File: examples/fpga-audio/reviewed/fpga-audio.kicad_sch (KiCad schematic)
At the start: 29 parts, among them J1 3V3 IN, J2 AUDIO OUT, J3 SPI PROG, U1 iCE40UP5K, U2 PCM5102A, U3 AP2112K-1.2, U4 W25Q32JV, X1 12MHz

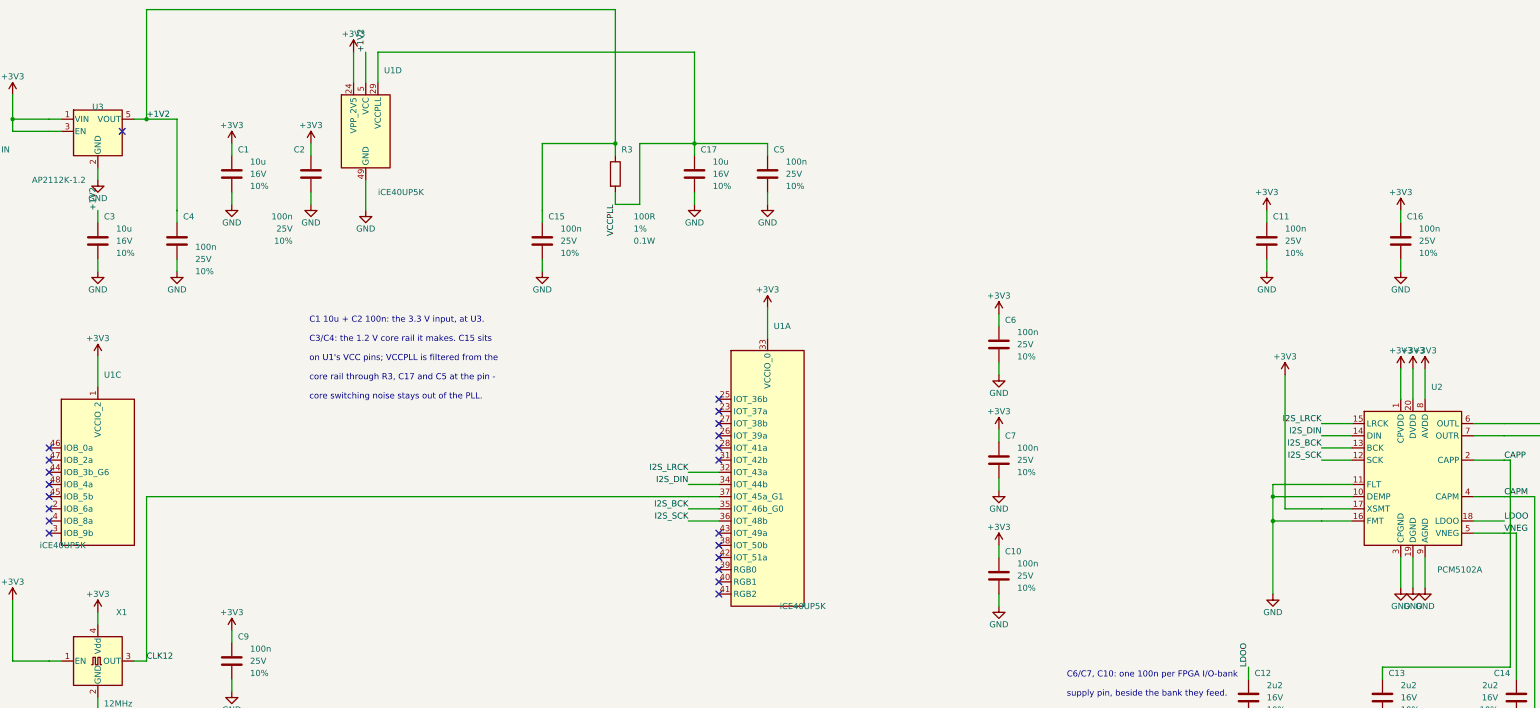
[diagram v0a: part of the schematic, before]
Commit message: Measure the copper that goes out and comes back, and the text drawn on text
The reviewer sent screenshots with circles on them. Two kinds: strings
printed through each other on the schematics, and copper that leaves a
pad, travels three sides of a rectangle and arrives four millimetres
away. Neither had a rule that could see it - `text_over_wire` measured
text against nets and nothing measured text against text, and
`route.detour` weighs a whole net, which averages one bad connection
away under any ratio worth setting.

New rule `route.wander`: one continuous run of copper - pad or junction
at each end - against the shortest way between those two ends that
clears the packages in between. The baseline walks the perimeter of
whatever the straight line crosses, so an opamp's feedback wrap is
measured against going round the package rather than through it. On
KiCad's 18 demo boards it fires once at the shipped 2.0x.

`readability.text_over_text` and `_over_wire` are regraded info: they
fire on 14 and 10 of those 18 human sheets. That is the estimate
talking, not the drawing. `ai-generated` still promotes both to errors,
so every generated design has to have none - and the five examples do.

What the two rules then made us fix:

* a net label's anchor cannot move, but its reading direction can. Each
  name is now offered the four quarters of its anchor and takes the
  first that prints over nothing. Power symbol names and PWR_FLAG names
  get the same treatment - four grounds on one row printed GNGNGNGND.
  Schematic text overlaps: buck 1, motor 2, carrier 1, fpga 7, all to 0.
* a plane crossing was priced at forty times front copper per
  millimetre, which is a prohibition, not a price: one millimetre of
  crossing bought a forty millimetre tour and the boards had grown
  them. Thirty is where neither `route.wander` nor `route.return_path`
  fires. Buck, motor and carrier now have no wander findings.
* `write_variant` resolves the routes a second time, so the
  straight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
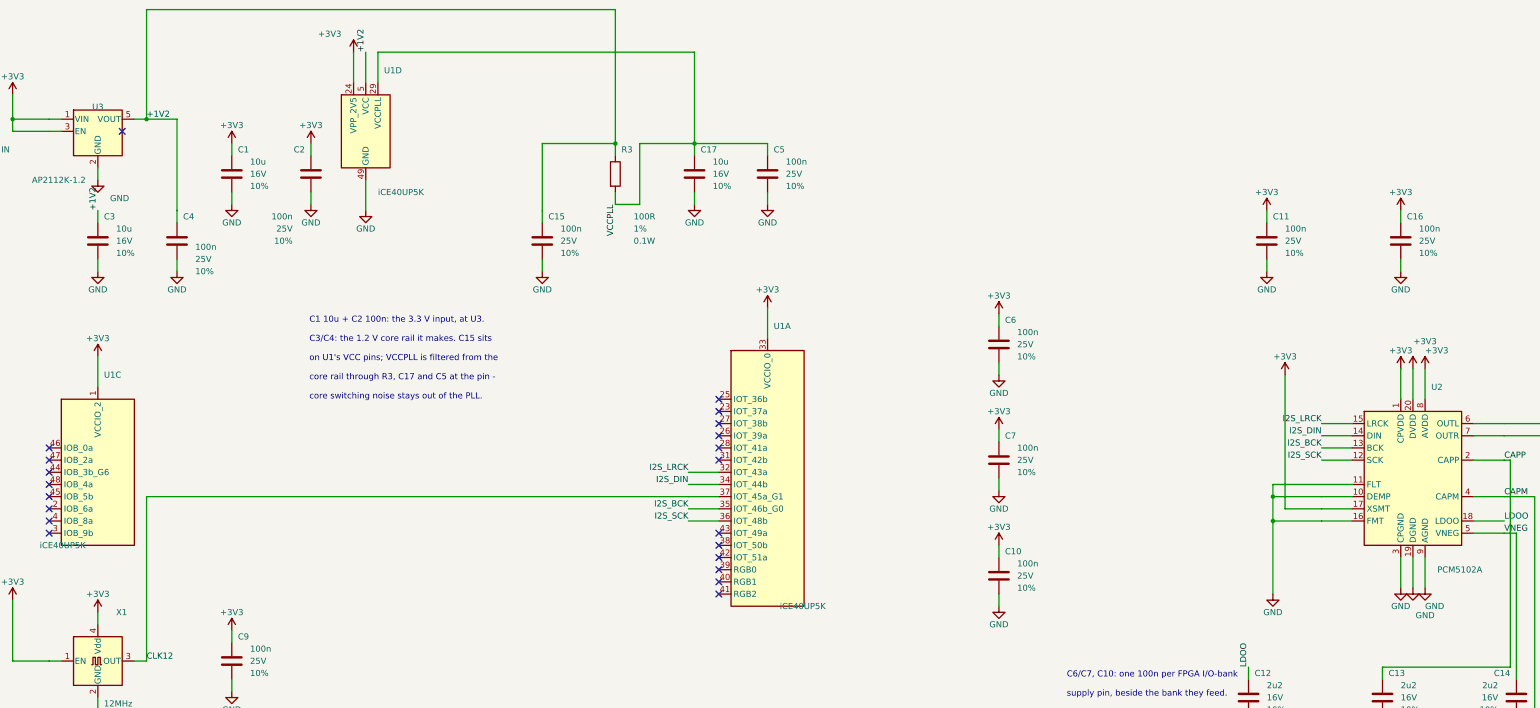
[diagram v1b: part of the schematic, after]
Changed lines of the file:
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@@
     (exclude_from_sim no) (in_bom no) (on_board yes) (dnp no)
     (property "Reference" "#PWR04" (at 109.22 22.86 0) (effects (font (size 1.27 1.27)) hide))
-    (property "Value" "+3V3" (at 109.22 19.05 0) (effects (font (size 1.27 1.27))))
+    (property "Value" "+3V3" (at 106.68 19.05 0) (effects (font (size 1.27 1.27)) (justify right)))
     (property "Footprint" "" (at 109.22 22.86 0) (effects (font (size 1.27 1.27)) hide))
     (property "Datasheet" "" (at 109.22 22.86 0) (effects (font (size 1.27 1.27)) hide))
@@
     (exclude_from_sim no) (in_bom no) (on_board yes) (dnp no)
     (property "Reference" "#PWR08" (at 330.2 88.9 0) (effects (font (size 1.27 1.27)) hide))
-    (property "Value" "+3V3" (at 330.2 85.09 0) (effects (font (size 1.27 1.27))))
+    (property "Value" "+3V3" (at 332.74 85.09 0) (effects (font (size 1.27 1.27)) (justify left)))
     (property "Footprint" "" (at 330.2 88.9 0) (effects (font (size 1.27 1.27)) hide))
     (property "Datasheet" "" (at 330.2 88.9 0) (effects (font (size 1.27 1.27)) hide))
@@
     (exclude_from_sim no) (in_bom no) (on_board yes) (dnp no)
     (property "Reference" "#PWR09" (at 330.2 134.62 0) (effects (font (size 1.27 1.27)) hide))
-    (property "Value" "GND" (at 330.2 138.43 0) (effects (font (size 1.27 1.27))))
+    (property "Value" "GND" (at 332.74 138.43 0) (effects (font (size 1.27 1.27)) (justify left)))
     (property "Footprint" "" (at 330.2 134.62 0) (effects (font (size 1.27 1.27)) hide))
     (property "Datasheet" "" (at 330.2 134.62 0) (effects (font (size 1.27 1.27)) hide))
@@
     (exclude_from_sim no) (in_bom no) (on_board yes) (dnp no)
     (property "Reference" "#PWR10" (at 332.74 88.9 0) (effects (font (size 1.27 1.27)) hide))
-    (property "Value" "+3V3" (at 332.74 85.09 0) (effects (font (size 1.27 1.27))))
+    (property "Value" "+3V3" (at 332.74 83.18 0) (effects (font (size 1.27 1.27))))
     (property "Footprint" "" (at 332.74 88.9 0) (effects (font (size 1.27 1.27)) hide))
     (property "Datasheet" "" (at 332.74 88.9 0) (effects (font (size 1.27 1.27)) hide))
@@
     (exclude_from_sim no) (in_bom no) (on_board yes) (dnp no)
     (property "Reference" "#PWR11" (at 332.74 134.62 0) (effects (font (size 1.27 1.27)) hide))
-    (property "Value" "GND" (at 332.74 138.43 0) (effects (font (size 1.27 1.27))))
+    (property "Value" "GND" (at 332.74 140.34 0) (effects (font (size 1.27 1.27))))
     (property "Footprint" "" (at 332.74 134.62 0) (effects (font (size 1.27 1.27)) hide))
     (property "Datasheet" "" (at 332.74 134.62 0) (effects (font (size 1.27 1.27)) hide))
@@
     (exclude_from_sim no) (in_bom no) (on_board yes) (dnp no)
     (property "Reference" "#PWR14" (at 55.88 49.53 0) (effects (font (size 1.27 1.27)) hide))
-    (property "Value" "GND" (at 55.88 53.34 0) (effects (font (size 1.27 1.27))))
+    (property "Value" "GND" (at 58.42 53.34 0) (effects (font (size 1.27 1.27)) (justify left)))
     (property "Footprint" "" (at 55.88 49.53 0) (effects (font (size 1.27 1.27)) hide))
     (property "Datasheet" "" (at 55.88 49.53 0) (effects (font (size 1.27 1.27)) hide))
